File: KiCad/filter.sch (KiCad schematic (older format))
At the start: 29 parts

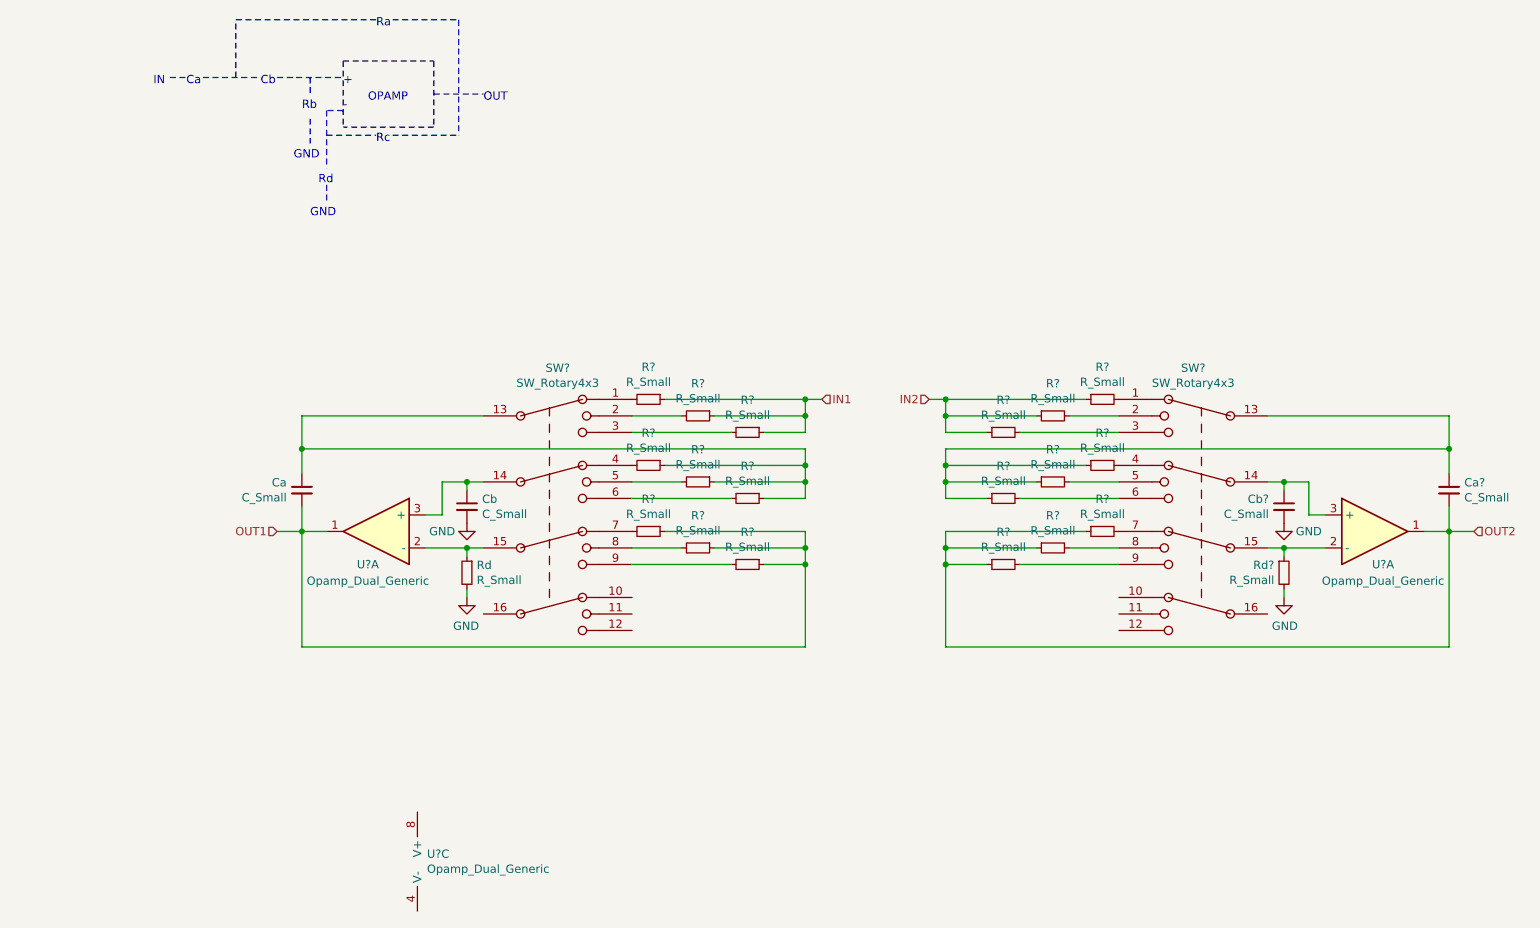
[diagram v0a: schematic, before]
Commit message: restored filter and added initial attenuation in trim
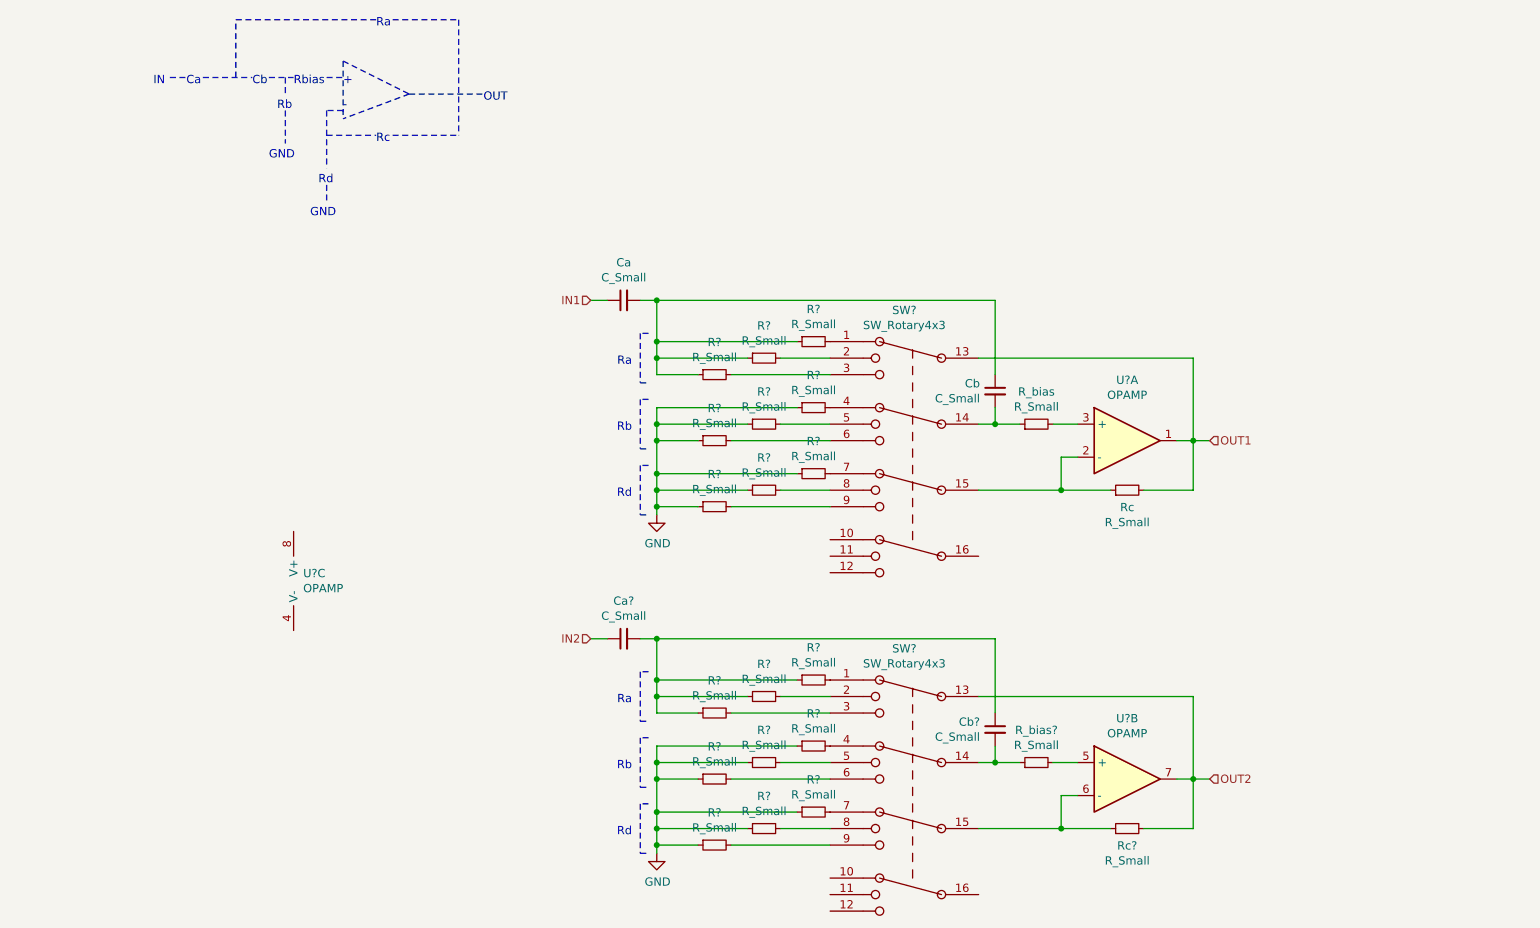
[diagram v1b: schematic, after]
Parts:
- removed Ca?, Cb?: C_Small, symbol Device:C_Small
- removed R? (x9), Rd, Rd?: R_Small, symbol Device:R_Small
- removed SW?: SW_Rotary4x3, symbol Switch:SW_Rotary4x3
- removed U?: Opamp_Dual_Generic, symbol Device:Opamp_Dual_Generic
- added Ca?, Cb?: C_Small, symbol Device:C_Small
- added R? (x9), R_bias, R_bias?, Rc, Rc?: R_Small, symbol Device:R_Small
- added SW?: SW_Rotary4x3, symbol Switch:SW_Rotary4x3
- added U?: OPAMP, symbol Device:Opamp_Dual_Generic
- U? (x2): value Opamp_Dual_Generic -> OPAMP
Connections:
- net GND: now also R?.1, R?.1, R?.1, R?.1, R?.1, R?.1, R?.1, R?.1, R?.1, R?.1, R?.1, R?.1; no longer Cb.2
- net IN1: now also Ca.1; no longer R?.1, R?.1, R?.1
- net IN2: now also Ca?.1
- net OUT1: now also SW?.13, Rc.2; no longer Ca.2, R?.1, R?.1, R?.1
- net OUT2: now also Rc?.2, SW?.13, U?.7
- net at SW?.15, U?.2 (-): now also Rc.1
- new net: Ca.2, Cb.1, R?.1, R?.1, R?.1
- new net: Cb.2, R_bias.1, SW?.14
- new net: R_bias.2, U?.3 (+)
- new net: Ca?.2, Cb?.1, R?.1, R?.1, R?.1
- new net: R?.2, SW?.1
- new net: Cb?.2, R_bias?.1, SW?.14
- new net: Rc?.1, SW?.15, U?.6 (-)
- new net: R?.2, SW?.2
- new net: R?.2, SW?.3
- new net: R?.2, SW?.4
- new net: R?.2, SW?.5
- new net: R?.2, SW?.6
- new net: R?.2, SW?.7
- new net: R?.2, SW?.8
- new net: R?.2, SW?.9
- new net: R_bias?.2, U?.5 (+)
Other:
- note added: "Rbias"
- note removed: "OPAMP"
- moved on the sheet: Ca, Cb, R?, SW?, U?A, U?C

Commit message: changed Q to a fixed value
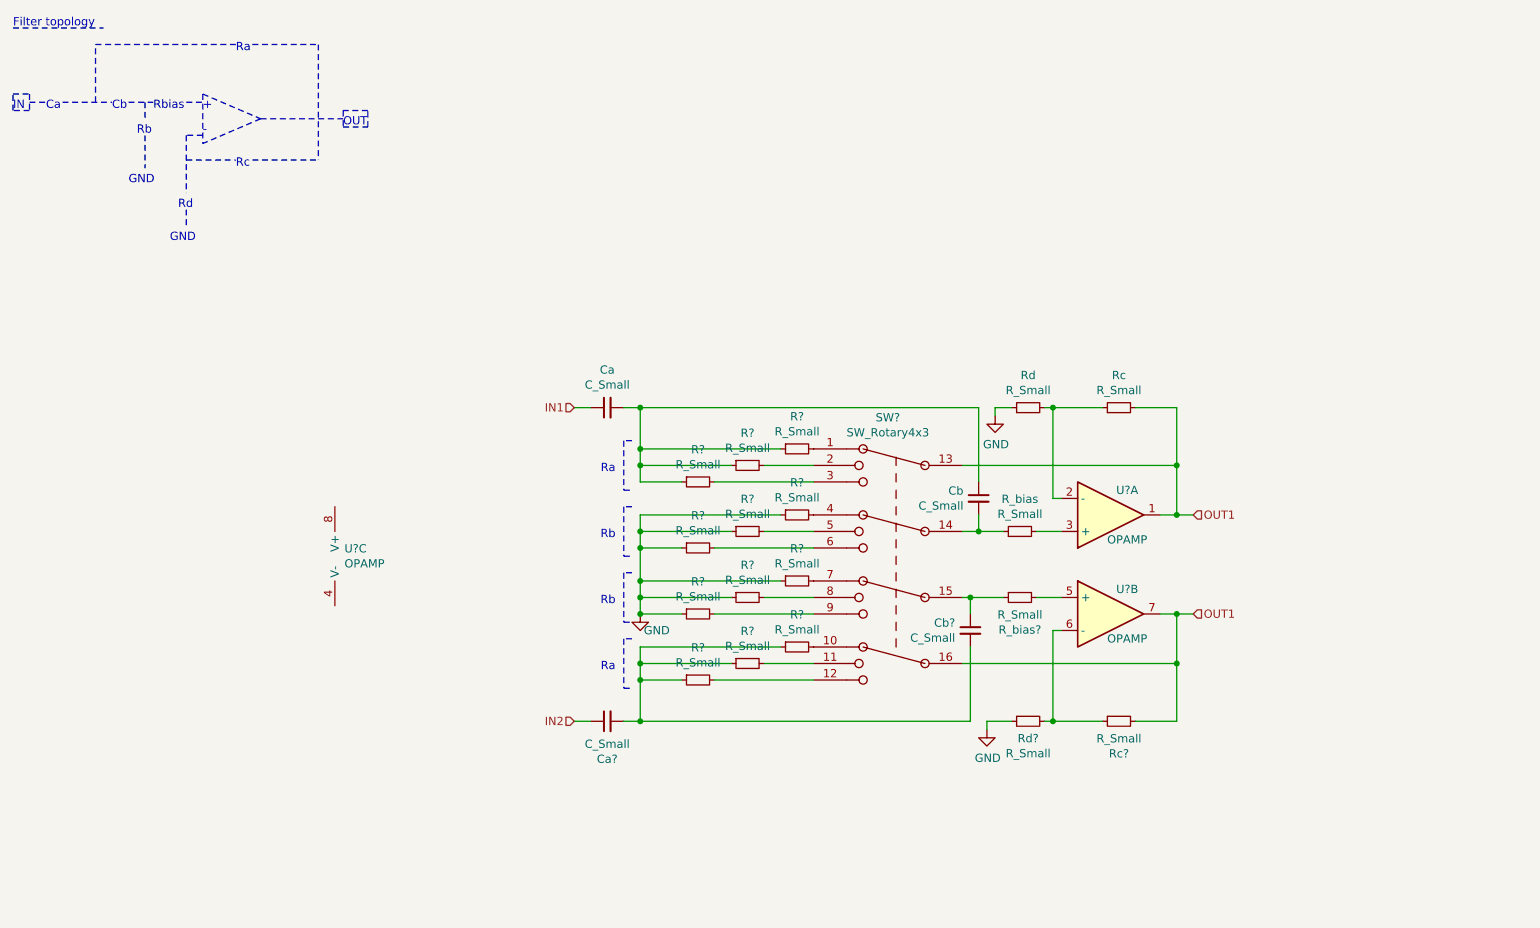
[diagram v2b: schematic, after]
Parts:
- removed Cb?: C_Small, symbol Device:C_Small
- removed R? (x9), R_bias?, Rc?: R_Small, symbol Device:R_Small
- removed SW?: SW_Rotary4x3, symbol Switch:SW_Rotary4x3
- added Cb?: C_Small, symbol Device:C_Small
- added R? (x3), R_bias?, Rc?, Rd, Rd?: R_Small, symbol Device:R_Small
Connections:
- net OUT2 is gone; now on net OUT1: U?.7
- net GND: now also R?.1, R?.1, R?.1, Rd.1, Rd?.1; no longer R?.1, R?.1, R?.1
- net OUT1: now also SW?.16, Rc?.2
- net at SW?.10: now also R?.2
- net at SW?.11: now also R?.2
- net at SW?.12: now also R?.2
- net at Rc.1, U?.2 (-): now also Rd.2; no longer SW?.15
- net at SW?.7: now also R?.2
- net at SW?.8: now also R?.2
- net at SW?.9: now also R?.2
- net at Ca?.2: now also R?.1, R?.1, R?.1, Cb?.2
- net at U?.6 (-): now also Rc?.1, Rd?.2
- net at U?.5 (+): now also R_bias?.2
- new net: Cb?.1, R_bias?.1, SW?.15
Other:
- note added: "Filter topology"
- moved on the sheet: Ca, Ca?, Cb, R?, R_bias, Rc, SW?, U?A, U?B, U?C

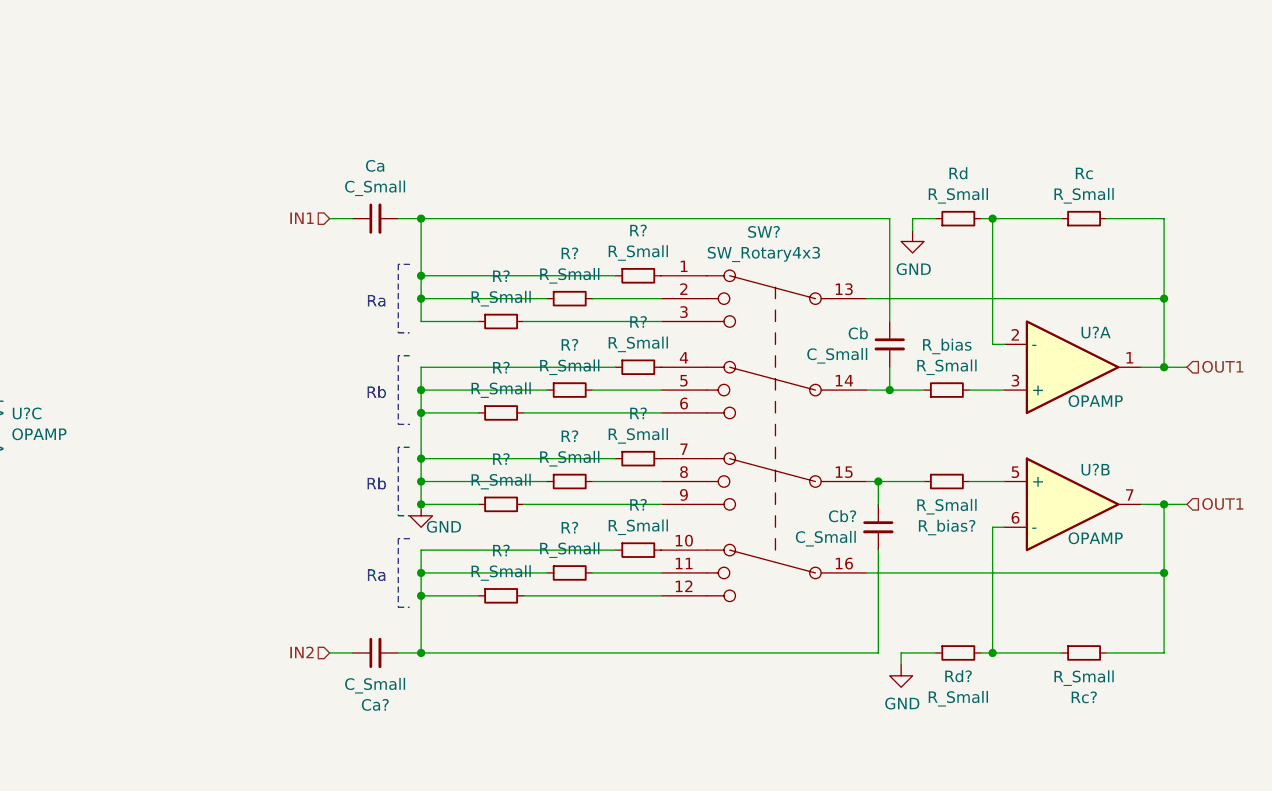
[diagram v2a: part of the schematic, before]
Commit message: moved initial attenuation to filter input
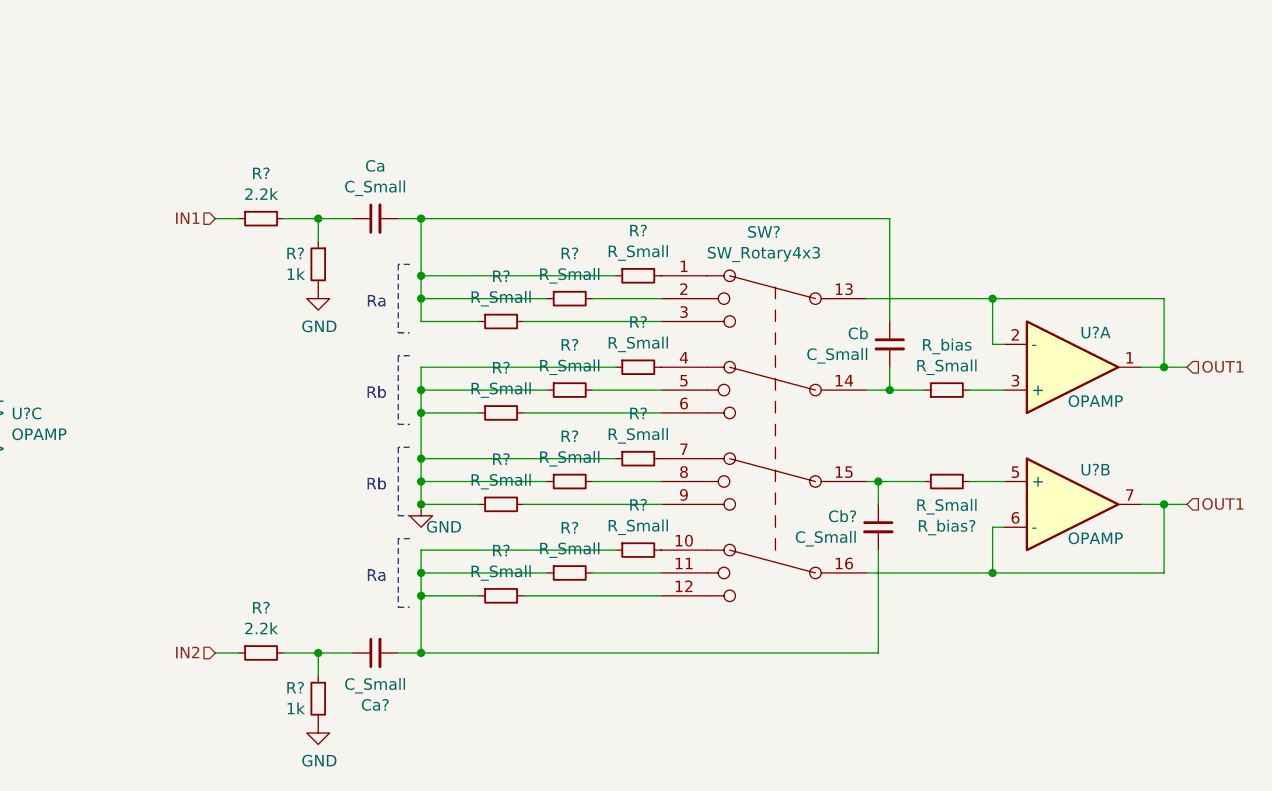
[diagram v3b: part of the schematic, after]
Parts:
- removed Rc, Rc?, Rd, Rd?: R_Small, symbol Device:R_Small
- added R? (x2): 2.2k, symbol Device:R_Small
- added R? (x2): 1k, symbol Device:R_Small
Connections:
- net GND: now also R?.2, R?.2
- net IN1: now also R?.1; no longer Ca.1
- net IN2: now also R?.1; no longer Ca?.1
- net OUT1: now also U?.2 (-), U?.6 (-)
- new net: Ca.1, R?.1, R?.2
- new net: Ca?.1, R?.1, R?.2
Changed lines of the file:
@@
 Text HLabel 7800 3700 2    50   Input ~ 0
 OUT1
-Text HLabel 4050 3050 0    50   Input ~ 0
+Text HLabel 3550 3050 0    50   Input ~ 0
 IN1
 $Comp
@@
 Connection ~ 4450 3300
 Wire Wire Line
-	4150 3050 4050 3050
-Wire Wire Line
-	7700 3400 7700 3700
-Wire Wire Line
 	7700 3700 7600 3700
 Wire Wire Line
@@
 Wire Wire Line
 	4450 3050 4450 3300
-$Comp
-L Device:R_Small Rc
-U 1 1 603EA424
-P 7350 3050
-F 0 "Rc" V 7546 3050 50  0000 C CNN
-F 1 "R_Small" V 7455 3050 50  0000 C CNN
-F 2 "" H 7350 3050 50  0001 C CNN
-F 3 "~" H 7350 3050 50  0001 C CNN
-	1    7350 3050
-	0    -1   -1   0
-$EndComp
 Connection ~ 7700 3700
 Wire Wire Line
 	7800 3700 7700 3700
-Wire Wire Line
-	7700 3400 6400 3400
 $Comp
 L Device:R_Small R_bias
@@
 Wire Wire Line
 	4350 4950 4450 4950
-Wire Wire Line
-	4150 4950 4050 4950
-Text HLabel 4050 4950 0    50   Input ~ 0
+Text HLabel 3550 4950 0    50   Input ~ 0
 IN2
 Wire Notes Line style solid
@@
 $EndComp
 Wire Wire Line
-	7450 3050 7700 3050
-Wire Wire Line
-	7700 3050 7700 3400
-Connection ~ 7700 3400
-Wire Wire Line
-	7250 3050 6950 3050
-Wire Wire Line
-	6950 3050 6950 3600
+	6950 3400 6950 3600
 Wire Wire Line
 	6950 3600 7000 3600
-$Comp
-L Device:R_Small Rd
-U 1 1 603F1291
-P 6800 3050
-F 0 "Rd" V 6996 3050 50  0000 C CNN
-F 1 "R_Small" V 6905 3050 50  0000 C CNN
-F 2 "" H 6800 3050 50  0001 C CNN
-F 3 "~" H 6800 3050 50  0001 C CNN
-	1    6800 3050
-	0    -1   -1   0
-$EndComp
-Wire Wire Line
-	6900 3050 6950 3050
-Connection ~ 6950 3050
-$Comp
-L power:GND #PWR?
-U 1 1 603F3286
-P 6600 3100
-F 0 "#PWR?" H 6600 2850 50  0001 C CNN
-F 1 "GND" H 6605 2927 50  0000 C CNN
-F 2 "" H 6600 3100 50  0001 C CNN
-F 3 "" H 6600 3100 50  0001 C CNN
-	1    6600 3100
-	1    0    0    -1
-$EndComp
-Wire Wire Line
-	6700 3050 6600 3050
-Wire Wire Line
-	6600 3050 6600 3100
 Wire Wire Line
 	4450 4300 4450 4200
@@
 OUT1
 Wire Wire Line
-	7700 4600 7700 4300
-Wire Wire Line
 	7700 4300 7600 4300
-$Comp
-L Device:R_Small Rc?
-U 1 1 6041A555
-P 7350 4950
-F 0 "Rc?" V 7546 4950 50  0000 C CNN
-F 1 "R_Small" V 7455 4950 50  0000 C CNN
-F 2 "" H 7350 4950 50  0001 C CNN
-F 3 "~" H 7350 4950 50  0001 C CNN
-	1    7350 4950
-	0    -1   1    0
-$EndComp
 Connection ~ 7700 4300
 Wire Wire Line
 	7800 4300 7700 4300
-Wire Wire Line
-	7700 4600 6400 4600
 $Comp
 L Device:R_Small R_bias?
@@
 	6850 4200 7000 4200
 Wire Wire Line
-	7450 4950 7700 4950
-Wire Wire Line
-	7700 4950 7700 4600
-Connection ~ 7700 4600
-Wire Wire Line
-	7250 4950 6950 4950
-Wire Wire Line
-	6950 4950 6950 4400
-Wire Wire Line
 	6950 4400 7000 4400
-$Comp
-L Device:R_Small Rd?
-U 1 1 6041A56C
-P 6800 4950
-F 0 "Rd?" V 6904 4950 50  0000 C CNN
-F 1 "R_Small" V 6995 4950 50  0000 C CNN
-F 2 "" H 6800 4950 50  0001 C CNN
-F 3 "~" H 6800 4950 50  0001 C CNN
-	1    6800 4950
-	0    -1   1    0
-$EndComp
-Wire Wire Line
-	6900 4950 6950 4950
-Connection ~ 6950 4950
 Wire Wire Line
 	4450 4950 4450 4700
@@
 Connection ~ 4450 3900
 Connection ~ 4450 4100
-$Comp
-L power:GND #PWR?
-U 1 1 6042ED4F
-P 6550 5000
-F 0 "#PWR?" H 6550 4750 50  0001 C CNN
-F 1 "GND" H 6555 4827 50  0000 C CNN
-F 2 "" H 6550 5000 50  0001 C CNN
-F 3 "" H 6550 5000 50  0001 C CNN
-	1    6550 5000
-	1    0    0    -1
-$EndComp
-Wire Wire Line
-	6550 5000 6550 4950
-Wire Wire Line
-	6550 4950 6700 4950
 Wire Notes Line
 	4400 4050 4350 4050
@@
 Wire Notes Line
 	2800 1250 2650 1250
+Wire Wire Line
+	6950 4600 7700 4600
+Wire Wire Line
+	7700 4300 7700 4600
+Wire Wire Line
+	6400 4600 6950 4600
+Connection ~ 6950 4600
+Wire Wire Line
+	6950 4600 6950 4400
+Wire Wire Line
+	6950 3400 7700 3400
+Wire Wire Line
+	7700 3400 7700 3700
+Wire Wire Line
+	6950 3400 6400 3400
+Connection ~ 6950 3400
+$Comp
+L Device:R_Small R?
+U 1 1 60412BF2
+P 3750 3050
+F 0 "R?" V 3554 3050 50  0000 C CNN
+F 1 "2.2k" V 3645 3050 50  0000 C CNN
+F 2 "" H 3750 3050 50  0001 C CNN
+F 3 "~" H 3750 3050 50  0001 C CNN
+	1    3750 3050
+	0    -1   1    0
+$EndComp
+Wire Wire Line
+	3650 3050 3550 3050
+Wire Wire Line
+	3850 3050 4000 3050
+$Comp
+L Device:R_Small R?
+U 1 1 60415A9E
+P 4000 3250
+F 0 "R?" H 4058 3296 50  0000 L CNN
+F 1 "1k" H 4058 3205 50  0000 L CNN
+F 2 "" H 4000 3250 50  0001 C CNN
+F 3 "~" H 4000 3250 50  0001 C CNN
+	1    4000 3250
+	-1   0    0    -1
+$EndComp
+Wire Wire Line
+	4000 3150 4000 3050
+Connection ~ 4000 3050
+Wire Wire Line
+	4000 3050 4150 3050
+$Comp
+L power:GND #PWR?
+U 1 1 6041757F
+P 4000 3350
+F 0 "#PWR?" H 4000 3100 50  0001 C CNN
+F 1 "GND" H 4005 3177 50  0000 C CNN
+F 2 "" H 4000 3350 50  0001 C CNN
+F 3 "" H 4000 3350 50  0001 C CNN
+	1    4000 3350
+	1    0    0    -1
+$EndComp
+$Comp
+L Device:R_Small R?
+U 1 1 60418D58
+P 3750 4950
+F 0 "R?" V 3554 4950 50  0000 C CNN
+F 1 "2.2k" V 3645 4950 50  0000 C CNN
+F 2 "" H 3750 4950 50  0001 C CNN
+F 3 "~" H 3750 4950 50  0001 C CNN
+	1    3750 4950
+	0    -1   1    0
+$EndComp
+Wire Wire Line
+	3650 4950 3550 4950
+Wire Wire Line
+	3850 4950 4000 4950
+$Comp
+L Device:R_Small R?
+U 1 1 60418D60
+P 4000 5150
+F 0 "R?" H 4058 5196 50  0000 L CNN
+F 1 "1k" H 4058 5105 50  0000 L CNN
+F 2 "" H 4000 5150 50  0001 C CNN
+F 3 "~" H 4000 5150 50  0001 C CNN
+	1    4000 5150
+	-1   0    0    -1
+$EndComp
+Wire Wire Line
+	4000 5050 4000 4950
+Connection ~ 4000 4950
+$Comp
+L power:GND #PWR?
+U 1 1 60418D69
+P 4000 5250
+F 0 "#PWR?" H 4000 5000 50  0001 C CNN
+F 1 "GND" H 4005 5077 50  0000 C CNN
+F 2 "" H 4000 5250 50  0001 C CNN
+F 3 "" H 4000 5250 50  0001 C CNN
+	1    4000 5250
+	1    0    0    -1
+$EndComp
+Wire Wire Line
+	4000 4950 4150 4950
 $EndSCHEMATC
